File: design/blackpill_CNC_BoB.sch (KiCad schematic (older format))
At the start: 295 parts, among them J101 ALimIN, J102 ZLimIN, J103 YLimIN, J104 XLimIN, J105 CS_IN, J106 FH_IN, J107 DoorIN, J108 ResetIN, J109 ProbeIN, J110 12V Power in, J111 AuxEncIn, J112 5V Power out, J113 ADC_in_1, J114 ADC_in_2, J115 stepDriverLim, J116 Reset, J117 UART1, J118 I2C, J119 SpindleVFD, J120 Spindle/Coolant, J121 Spindle, J122 Coolant, J123 AuxOut, J124 XStepDrv, J125 YStepDrv, J126 ZStepDrv, J127 AStepDrv, U101 TLP290-4, U102 TLP290-4, U103 TLP290-4, U104 74LVC2G17, U105 LD1117S50TR_SOT223, U106 LM358, U107 TLV9001, U108 TLV9001, U109 YAAJ_WeAct_BlackPill_Part_Like, U110 TLV9001, U111 TLV9001, U112 74HCT541, U113 74HCT541, U114 74HCT541, U115 ULN2003A, U116 ULN2003A, U117 ULN2003A

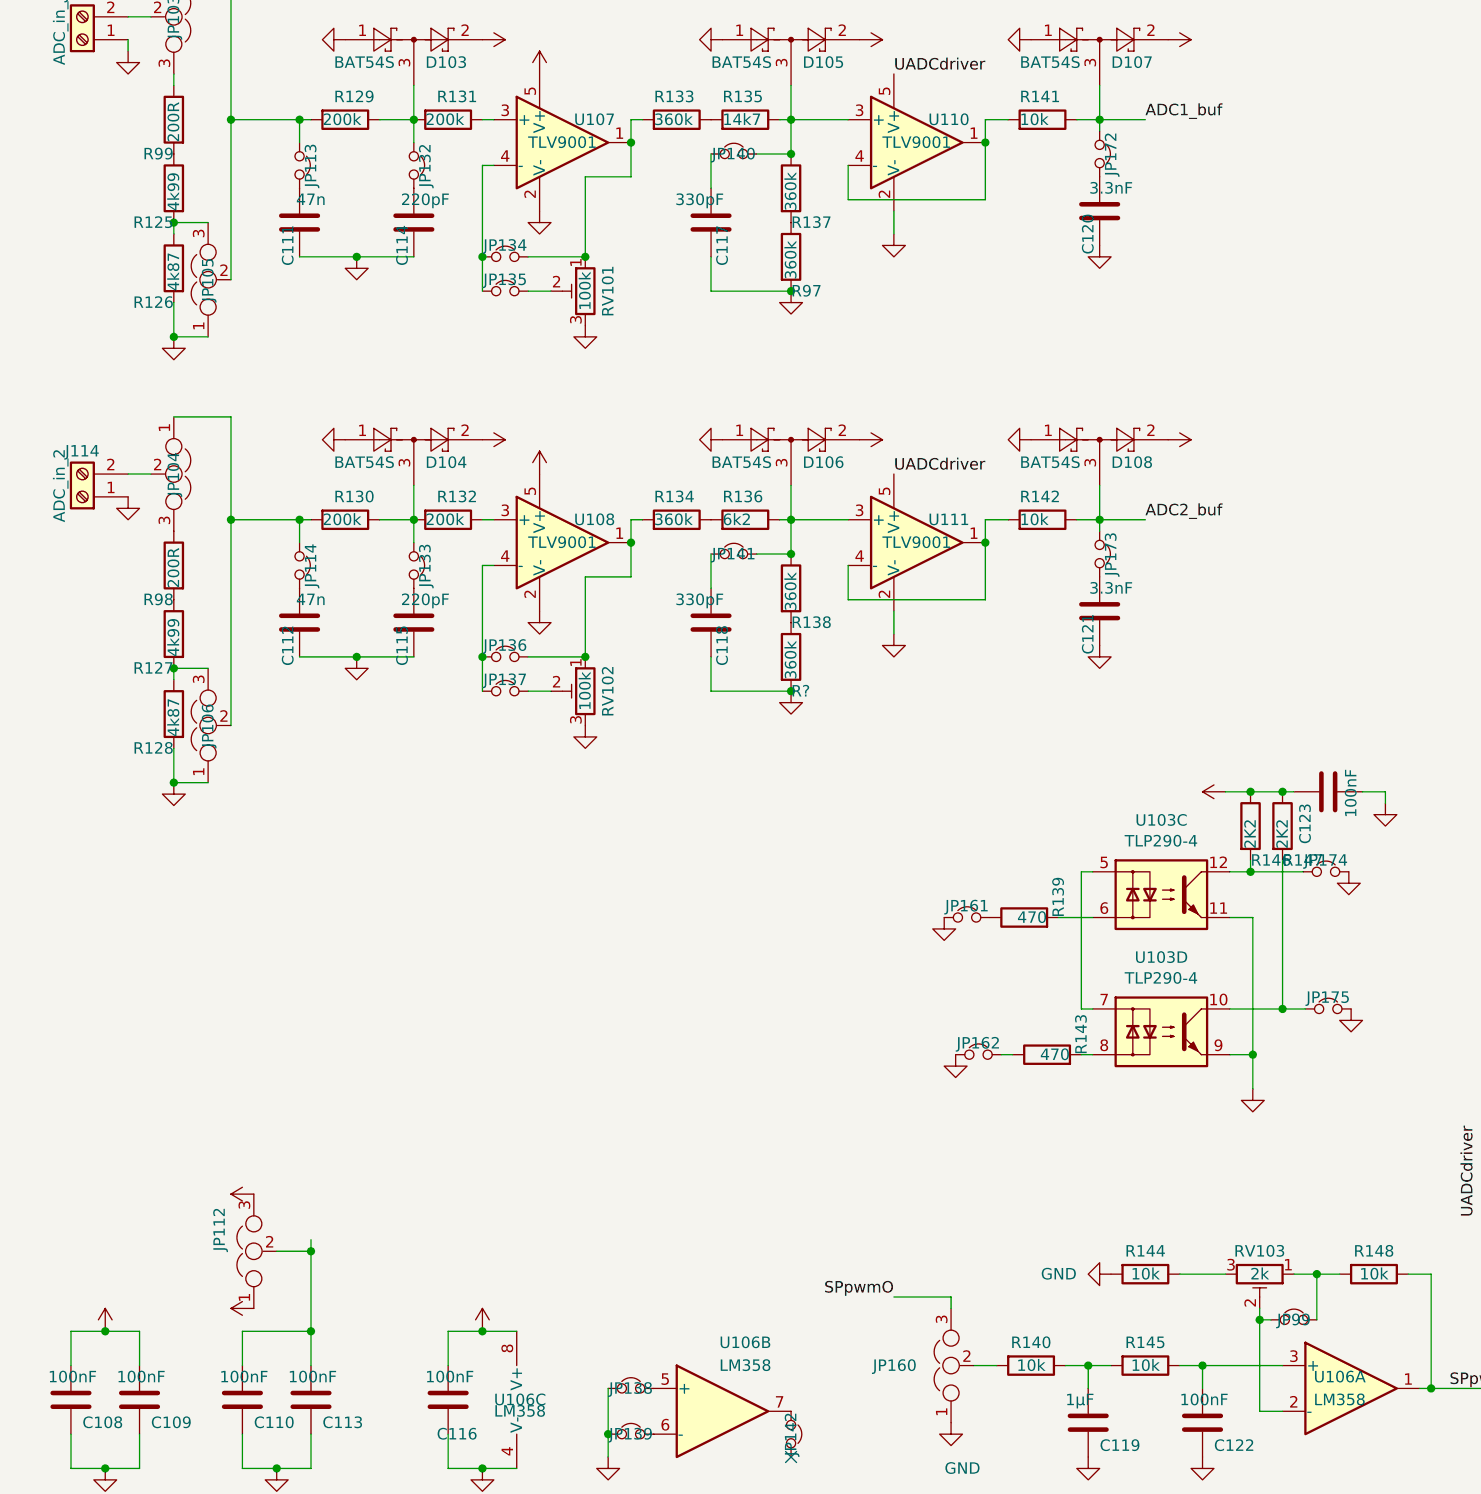
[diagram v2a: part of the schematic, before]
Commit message: rework footprints
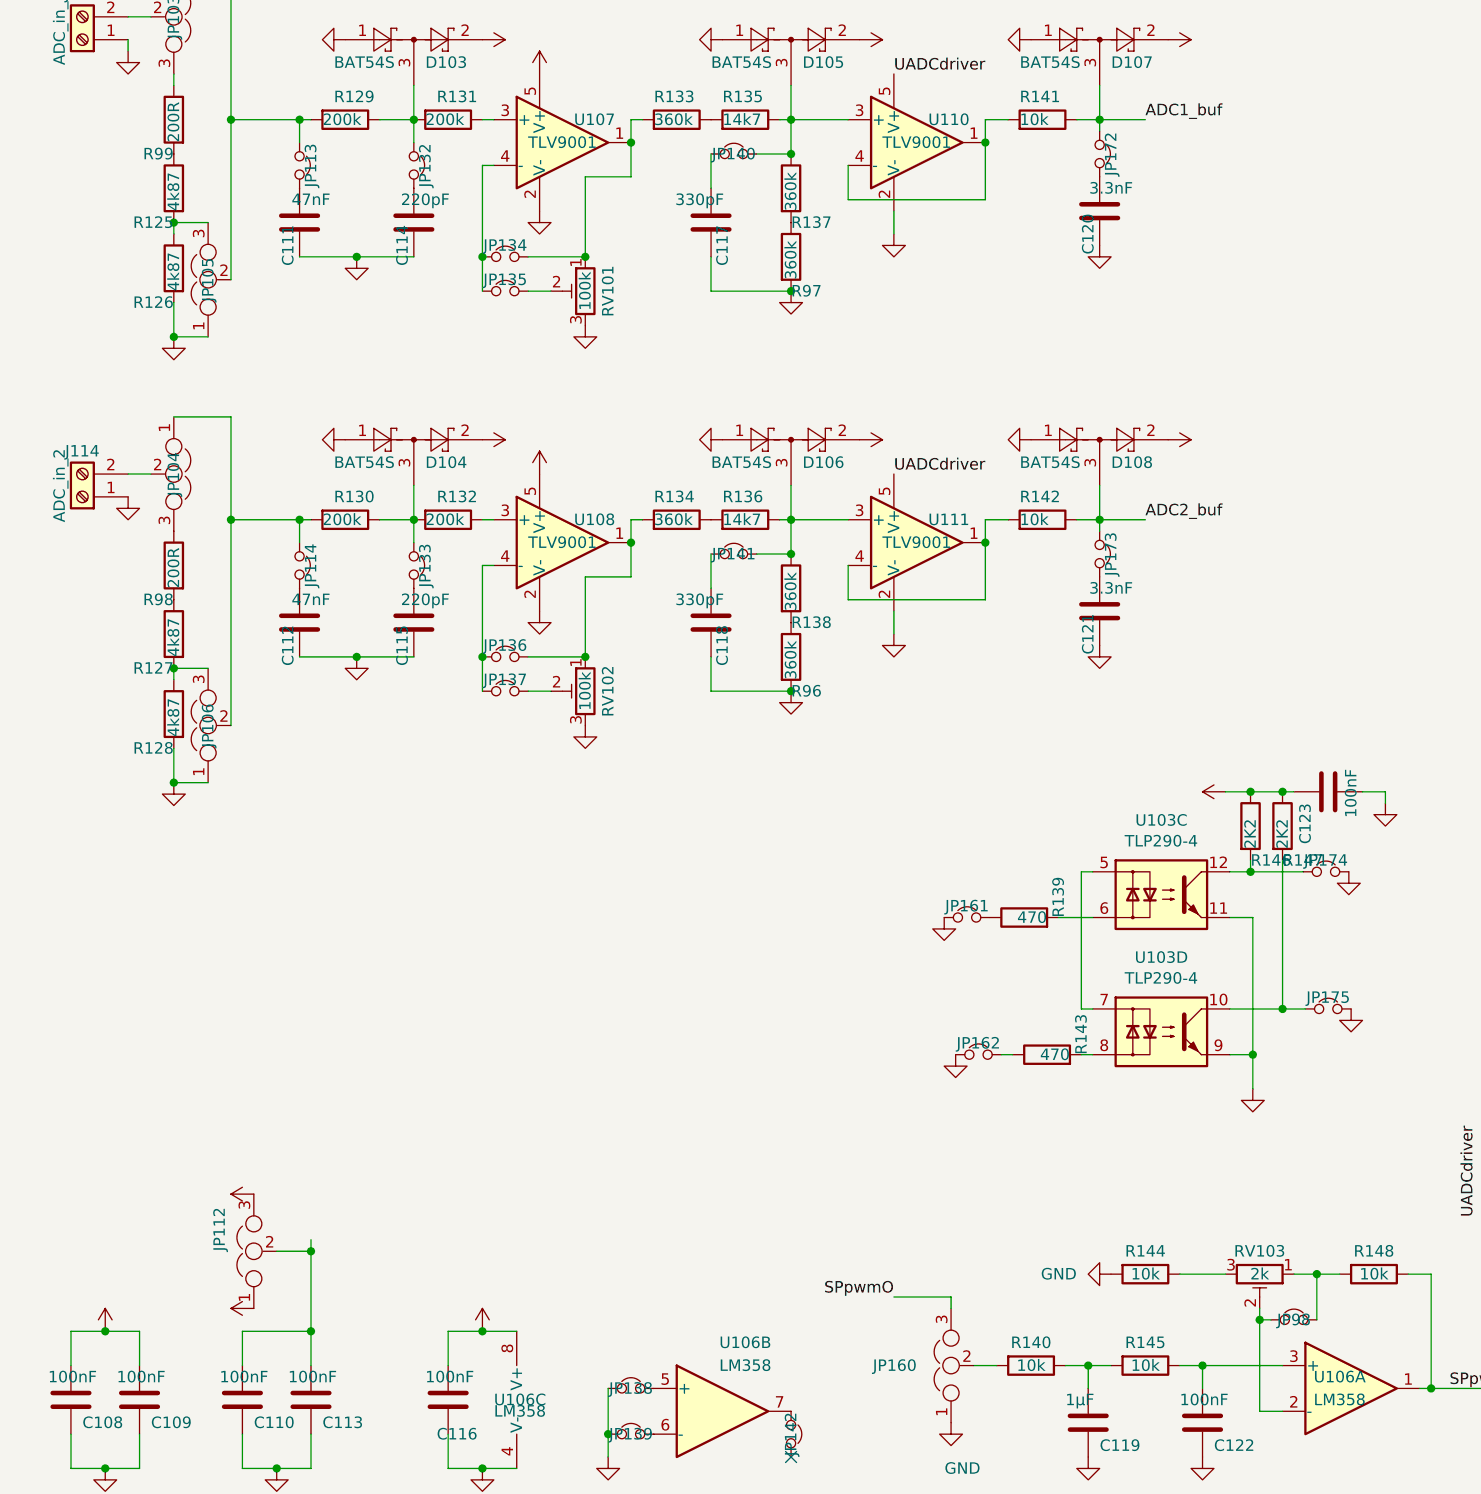
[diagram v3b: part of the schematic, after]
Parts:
- C102: footprint Capacitor_THT:CP_Axial_L29.0mm_D16.0mm_P35.00mm_Horizontal -> Capacitor_SMD:CP_Elec_10x10
- C104: footprint Capacitor_SMD:C_1206_3216Metric -> Capacitor_SMD:CP_Elec_10x10
- C111, C112: value 47n -> 47nF
- C119: footprint (none) -> Capacitor_SMD:C_0603_1608Metric
- C98, C99: footprint Capacitor_SMD:C_0603_1608Metric -> Capacitor_SMD:C_1206_3216Metric
- R125, R127: value 4k99 -> 4k87; footprint (none) -> Resistor_SMD:R_0805_2012Metric
- R126, R128: footprint (none) -> Resistor_SMD:R_0805_2012Metric
- R133, R134, R137, R138, R97, R98, R99: footprint (none) -> Resistor_SMD:R_0603_1608Metric
- R135: footprint (none) -> Resistor_SMD:R_0402_1005Metric
- R136: value 6k2 -> 14k7; footprint (none) -> Resistor_SMD:R_0402_1005Metric
- R96: renamed from R?; footprint (none) -> Resistor_SMD:R_0603_1608Metric
- U104: footprint (none) -> Package_TO_SOT_SMD:SOT-23-6
- U106: footprint (none) -> Package_SO:SOIC-8_3.9x4.9mm_P1.27mm
- U109: footprint (none) -> Footprints:YAAJ_WeAct_BlackPill_2
- U112, U113, U114: footprint (none) -> Package_SO:TSSOP-20_4.4x6.5mm_P0.65mm
- U115, U116, U117: footprint (none) -> Package_SO:SOIC-16_3.9x9.9mm_P1.27mm
- renumbered JP99 to JP98
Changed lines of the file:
@@
 F 0 "U104" H 1850 8550 40  0000 C CNN
 F 1 "74LVC2G17" H 2050 8650 40  0000 C CNN
-F 2 "" H 1995 8415 30  0001 C CNN
+F 2 "Package_TO_SOT_SMD:SOT-23-6" H 1995 8415 30  0001 C CNN
 F 3 "" H 2045 8665 60  0000 C CNN
 	2    1900 8550
@@
 F 0 "U104" H 1900 8000 40  0000 C CNN
 F 1 "74LVC2G17" H 2100 7900 40  0000 C CNN
-F 2 "" H 1900 8208 30  0001 C CNN
+F 2 "Package_TO_SOT_SMD:SOT-23-6" H 1900 8208 30  0001 C CNN
 F 3 "" H 2045 8115 60  0000 C CNN
 	1    1900 8000
@@
 F 0 "U109" H 7050 3360 50  0000 C CNN
 F 1 "YAAJ_WeAct_BlackPill_Part_Like" H 7050 3260 50  0000 C CNN
-F 2 "" H 7050 1000 50  0001 C CNN
+F 2 "Footprints:YAAJ_WeAct_BlackPill_2" H 7050 1000 50  0001 C CNN
 F 3 "" H 7740 1180 50  0001 C CNN
 	1    7040 2180
@@
 F 0 "U115" H 13500 2280 50  0000 C CNN
 F 1 "ULN2003A" H 13800 1000 50  0000 C CNN
-F 2 "" H 13550 1050 50  0001 L CNN
+F 2 "Package_SO:SOIC-16_3.9x9.9mm_P1.27mm" H 13550 1050 50  0001 L CNN
 F 3 "" H 13600 1400 50  0001 C CNN
 	1    13500 1600
@@
 F 0 "U112" H 11900 2900 50  0000 C CNN
 F 1 "74HCT541" H 11900 2800 50  0000 C CNN
-F 2 "" H 11900 1900 50  0001 C CNN
+F 2 "Package_SO:TSSOP-20_4.4x6.5mm_P0.65mm" H 11900 1900 50  0001 C CNN
 F 3 "http://www.ti.com/lit/gpn/sn74HCT541" H 11900 1900 50  0001 C CNN
 	1    11900 1900
@@
 F 0 "U116" H 13500 4680 50  0000 C CNN
 F 1 "ULN2003A" H 13400 4450 50  0000 C CNN
-F 2 "" H 13550 3450 50  0001 L CNN
+F 2 "Package_SO:SOIC-16_3.9x9.9mm_P1.27mm" H 13550 3450 50  0001 L CNN
 F 3 "" H 13600 3800 50  0001 C CNN
 	1    13500 4000
@@
 F 0 "U113" H 11900 5300 50  0000 C CNN
 F 1 "74HCT541" H 11900 5200 50  0000 C CNN
-F 2 "" H 11900 4300 50  0001 C CNN
+F 2 "Package_SO:TSSOP-20_4.4x6.5mm_P0.65mm" H 11900 4300 50  0001 C CNN
 F 3 "http://www.ti.com/lit/gpn/sn74HCT541" H 11900 4300 50  0001 C CNN
 	1    11900 4300
@@
 F 0 "U117" H 13850 7480 50  0000 C CNN
 F 1 "ULN2003A" H 14150 6200 50  0000 C CNN
-F 2 "" H 13900 6250 50  0001 L CNN
+F 2 "Package_SO:SOIC-16_3.9x9.9mm_P1.27mm" H 13900 6250 50  0001 L CNN
 F 3 "" H 13950 6600 50  0001 C CNN
 	1    13850 6800
@@
 F 0 "U114" H 11950 7400 50  0000 C CNN
 F 1 "74HCT541" H 11950 6800 50  0000 C CNN
-F 2 "" H 11950 7100 50  0001 C CNN
+F 2 "Package_SO:TSSOP-20_4.4x6.5mm_P0.65mm" H 11950 7100 50  0001 C CNN
 F 3 "http://www.ti.com/lit/gpn/sn74HCT541" H 11950 7100 50  0001 C CNN
 	1    11950 7100
@@
 F 0 "U106" H 10100 10400 50  0000 C CNN
 F 1 "LM358" H 10100 10300 50  0000 C CNN
-F 2 "" H 10150 10350 50  0001 C CNN
+F 2 "Package_SO:SOIC-8_3.9x4.9mm_P1.27mm" H 10150 10350 50  0001 C CNN
 F 3 "http://www.ti.com/lit/ds/symlink/lm2904-n.pdf" H 10150 10350 50  0001 C CNN
 	1    10150 10350
@@
 F 0 "U106" H 7500 10750 50  0000 C CNN
 F 1 "LM358" H 7500 10650 50  0000 C CNN
-F 2 "" H 7400 10450 50  0001 C CNN
+F 2 "Package_SO:SOIC-8_3.9x4.9mm_P1.27mm" H 7400 10450 50  0001 C CNN
 F 3 "http://www.ti.com/lit/ds/symlink/lm2904-n.pdf" H 7400 10450 50  0001 C CNN
 	2    7400 10450
@@
 F 0 "U106" H 6400 10400 50  0000 L CNN
 F 1 "LM358" H 6400 10350 50  0000 L CNN
-F 2 "" H 6600 10400 50  0001 C CNN
+F 2 "Package_SO:SOIC-8_3.9x4.9mm_P1.27mm" H 6600 10400 50  0001 C CNN
 F 3 "http://www.ti.com/lit/ds/symlink/lm2904-n.pdf" H 6600 10400 50  0001 C CNN
 	3    6600 10400
@@
 F 0 "C119" H 9050 10400 50  0000 L CNN
 F 1 "1µF" H 8900 10600 50  0000 L CNN
-F 2 "" H 9038 10350 50  0001 C CNN
+F 2 "Capacitor_SMD:C_0603_1608Metric" H 9038 10350 50  0001 C CNN
 F 3 "~" H 9000 10500 50  0001 C CNN
 	1    9000 10500
@@
 F 0 "C102" H 1600 10000 50  0000 L CNN
 F 1 "470µF" H 1550 10200 50  0000 L CNN
-F 2 "Capacitor_THT:CP_Axial_L29.0mm_D16.0mm_P35.00mm_Horizontal" H 1688 9950 50  0001 C CNN
+F 2 "Capacitor_SMD:CP_Elec_10x10" H 1688 9950 50  0001 C CNN
 F 3 "~" H 1650 10100 50  0001 C CNN
 	1    1650 10100
@@
 F 0 "C104" H 2900 10000 50  0000 L CNN
 F 1 "470µF" H 2850 10250 50  0000 L CNN
-F 2 "Capacitor_SMD:C_1206_3216Metric" H 2988 9950 50  0001 C CNN
+F 2 "Capacitor_SMD:CP_Elec_10x10" H 2988 9950 50  0001 C CNN
 F 3 "~" H 2950 10100 50  0001 C CNN
 	1    2950 10100
@@
 F 0 "R133" V 7300 4700 50  0000 L CNN
 F 1 "360k" V 7200 4700 50  0000 L CNN
-F 2 "" V 7130 4800 50  0001 C CNN
+F 2 "Resistor_SMD:R_0603_1608Metric" V 7130 4800 50  0001 C CNN
 F 3 "~" H 7200 4800 50  0001 C CNN
 	1    7200 4800
@@
 F 0 "R137" H 7700 4950 50  0000 L CNN
 F 1 "360k" V 7700 5000 50  0000 L CNN
-F 2 "" V 7630 5100 50  0001 C CNN
+F 2 "Resistor_SMD:R_0603_1608Metric" V 7630 5100 50  0001 C CNN
 F 3 "~" H 7700 5100 50  0001 C CNN
 	1    7700 5100
@@
 P 5550 5250
 F 0 "C111" V 5600 5150 50  0000 C CNN
-F 1 "47n" H 5500 5350 50  0000 C CNN
+F 1 "47nF" H 5500 5350 50  0000 C CNN
 F 2 "Capacitor_SMD:C_0603_1608Metric" H 5588 5100 50  0001 C CNN
 F 3 "~" H 5550 5250 50  0001 C CNN
@@
 P 5000 5100
 F 0 "R125" H 5000 4950 50  0000 L CNN
-F 1 "4k99" V 5000 5000 50  0000 L CNN
-F 2 "" V 4930 5100 50  0001 C CNN
+F 1 "4k87" V 5000 5000 50  0000 L CNN
+F 2 "Resistor_SMD:R_0805_2012Metric" V 4930 5100 50  0001 C CNN
 F 3 "~" H 5000 5100 50  0001 C CNN
 	1    5000 5100
@@
 F 0 "R126" H 5000 5300 50  0000 L CNN
 F 1 "4k87" V 5000 5350 50  0000 L CNN
-F 2 "" V 4930 5450 50  0001 C CNN
+F 2 "Resistor_SMD:R_0805_2012Metric" V 4930 5450 50  0001 C CNN
 F 3 "~" H 5000 5450 50  0001 C CNN
 	1    5000 5450
@@
 F 0 "R135" V 7600 4700 50  0000 L CNN
 F 1 "14k7" V 7500 4700 50  0000 L CNN
-F 2 "" V 7430 4800 50  0001 C CNN
+F 2 "Resistor_SMD:R_0402_1005Metric" V 7430 4800 50  0001 C CNN
 F 3 "~" H 7500 4800 50  0001 C CNN
 	1    7500 4800
@@
 F 0 "R134" V 7300 6450 50  0000 L CNN
 F 1 "360k" V 7200 6450 50  0000 L CNN
-F 2 "" V 7130 6550 50  0001 C CNN
+F 2 "Resistor_SMD:R_0603_1608Metric" V 7130 6550 50  0001 C CNN
 F 3 "~" H 7200 6550 50  0001 C CNN
 	1    7200 6550
@@
 F 0 "R138" H 7700 6700 50  0000 L CNN
 F 1 "360k" V 7700 6750 50  0000 L CNN
-F 2 "" V 7630 6850 50  0001 C CNN
+F 2 "Resistor_SMD:R_0603_1608Metric" V 7630 6850 50  0001 C CNN
 F 3 "~" H 7700 6850 50  0001 C CNN
 	1    7700 6850
@@
 P 5550 7000
 F 0 "C112" V 5600 6900 50  0000 C CNN
-F 1 "47n" H 5500 7100 50  0000 C CNN
+F 1 "47nF" H 5500 7100 50  0000 C CNN
 F 2 "Capacitor_SMD:C_0603_1608Metric" H 5588 6850 50  0001 C CNN
 F 3 "~" H 5550 7000 50  0001 C CNN
@@
 P 5000 7050
 F 0 "R127" H 5000 6900 50  0000 L CNN
-F 1 "4k99" V 5000 6950 50  0000 L CNN
-F 2 "" V 4930 7050 50  0001 C CNN
+F 1 "4k87" V 5000 6950 50  0000 L CNN
+F 2 "Resistor_SMD:R_0805_2012Metric" V 4930 7050 50  0001 C CNN
 F 3 "~" H 5000 7050 50  0001 C CNN
 	1    5000 7050
@@
 F 0 "R128" H 5000 7250 50  0000 L CNN
 F 1 "4k87" V 5000 7300 50  0000 L CNN
-F 2 "" V 4930 7400 50  0001 C CNN
+F 2 "Resistor_SMD:R_0805_2012Metric" V 4930 7400 50  0001 C CNN
 F 3 "~" H 5000 7400 50  0001 C CNN
 	1    5000 7400
@@
 P 7500 6550
 F 0 "R136" V 7600 6450 50  0000 L CNN
-F 1 "6k2" V 7500 6450 50  0000 L CNN
-F 2 "" V 7430 6550 50  0001 C CNN
+F 1 "14k7" V 7500 6450 50  0000 L CNN
+F 2 "Resistor_SMD:R_0402_1005Metric" V 7430 6550 50  0001 C CNN
 F 3 "~" H 7500 6550 50  0001 C CNN
 	1    7500 6550
@@
 	1200 7830 1200 8100
 $Comp
-L Device:Jumper_NC_Small JP99
+L Device:Jumper_NC_Small JP98
 U 1 1 66C69E3B
 P 9900 10050
-F 0 "JP99" H 9900 10050 50  0000 C CNN
+F 0 "JP98" H 9900 10050 50  0000 C CNN
 F 1 "Jumper_NC_Small" H 9900 10200 50  0001 C CNN
 F 2 "Connector_PinHeader_2.54mm:PinHeader_1x02_P2.54mm_Vertical" H 9900 10050 50  0001 C CNN
@@
 F 0 "C99" H 1900 10000 50  0000 L CNN
 F 1 "22µF" H 1850 10250 50  0000 L CNN
-F 2 "Capacitor_SMD:C_0603_1608Metric" H 1988 9950 50  0001 C CNN
+F 2 "Capacitor_SMD:C_1206_3216Metric" H 1988 9950 50  0001 C CNN
 F 3 "~" H 1950 10100 50  0001 C CNN
 	1    1950 10100
@@
 F 0 "C98" H 3150 10000 50  0000 L CNN
 F 1 "47µF" H 3100 10200 50  0000 L CNN
-F 2 "Capacitor_SMD:C_0603_1608Metric" H 3238 9950 50  0001 C CNN
+F 2 "Capacitor_SMD:C_1206_3216Metric" H 3238 9950 50  0001 C CNN
 F 3 "~" H 3200 10100 50  0001 C CNN
 	1    3200 10100
@@
 F 0 "R99" H 5000 4650 50  0000 L CNN
 F 1 "200R" V 5000 4700 50  0000 L CNN
-F 2 "" V 4930 4800 50  0001 C CNN
+F 2 "Resistor_SMD:R_0603_1608Metric" V 4930 4800 50  0001 C CNN
 F 3 "~" H 5000 4800 50  0001 C CNN
 	1    5000 4800
@@
 F 0 "R98" H 5000 6600 50  0000 L CNN
 F 1 "200R" V 5000 6650 50  0000 L CNN
-F 2 "" V 4930 6750 50  0001 C CNN
+F 2 "Resistor_SMD:R_0603_1608Metric" V 4930 6750 50  0001 C CNN
 F 3 "~" H 5000 6750 50  0001 C CNN
 	1    5000 6750
@@
 F 0 "R97" H 7700 5250 50  0000 L CNN
 F 1 "360k" V 7700 5300 50  0000 L CNN
-F 2 "" V 7630 5400 50  0001 C CNN
+F 2 "Resistor_SMD:R_0603_1608Metric" V 7630 5400 50  0001 C CNN
 F 3 "~" H 7700 5400 50  0001 C CNN
 	1    7700 5400
@@
 	7350 5100 7350 4950
 $Comp
-L Device:R R?
+L Device:R R96
 U 1 1 677A4CC0
 P 7700 7150
-F 0 "R?" H 7700 7000 50  0000 L CNN
+F 0 "R96" H 7700 7000 50  0000 L CNN
 F 1 "360k" V 7700 7050 50  0000 L CNN
-F 2 "" V 7630 7150 50  0001 C CNN
+F 2 "Resistor_SMD:R_0603_1608Metric" V 7630 7150 50  0001 C CNN
 F 3 "~" H 7700 7150 50  0001 C CNN
 	1    7700 7150
